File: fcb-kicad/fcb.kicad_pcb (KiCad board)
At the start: 4 copper layers, 45 x 45 mm, 90 parts, among them J1 Conn_ESC_4in1, J10 AI_5V_2, J11 AI_3V, J2 SWD, J3 Conn_Coaxial, J4 I2C, J5 USB_B_Micro, J6 PB9, J7 PB13, J8 UART, J9 AI_5V_1, Q1 S8050 J3Y, SW1 SW_Push, SW3 BTN_USER, U1 STM32F411CEUx, U2 TPS5430DDA, U3 AMS1117-3.3, U4 W25Q128JVS, U5 LSM6DS3, U6 DL-RTS4432, U7 BMP388, U8 QMC5883L, U9 USBLC6-2SC6, Y1 16 MHz

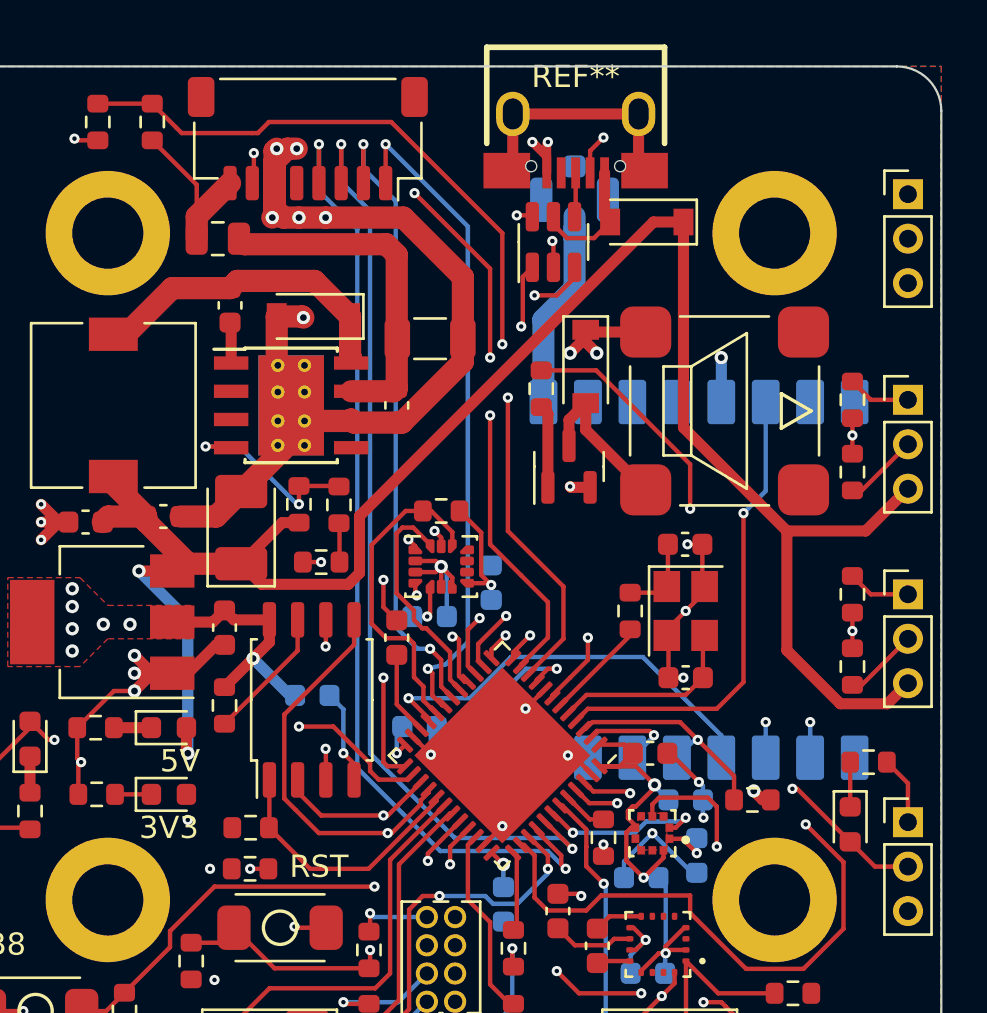
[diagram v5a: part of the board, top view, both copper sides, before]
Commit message: USB diffpair to bottom layer for more continous 3V3 fill
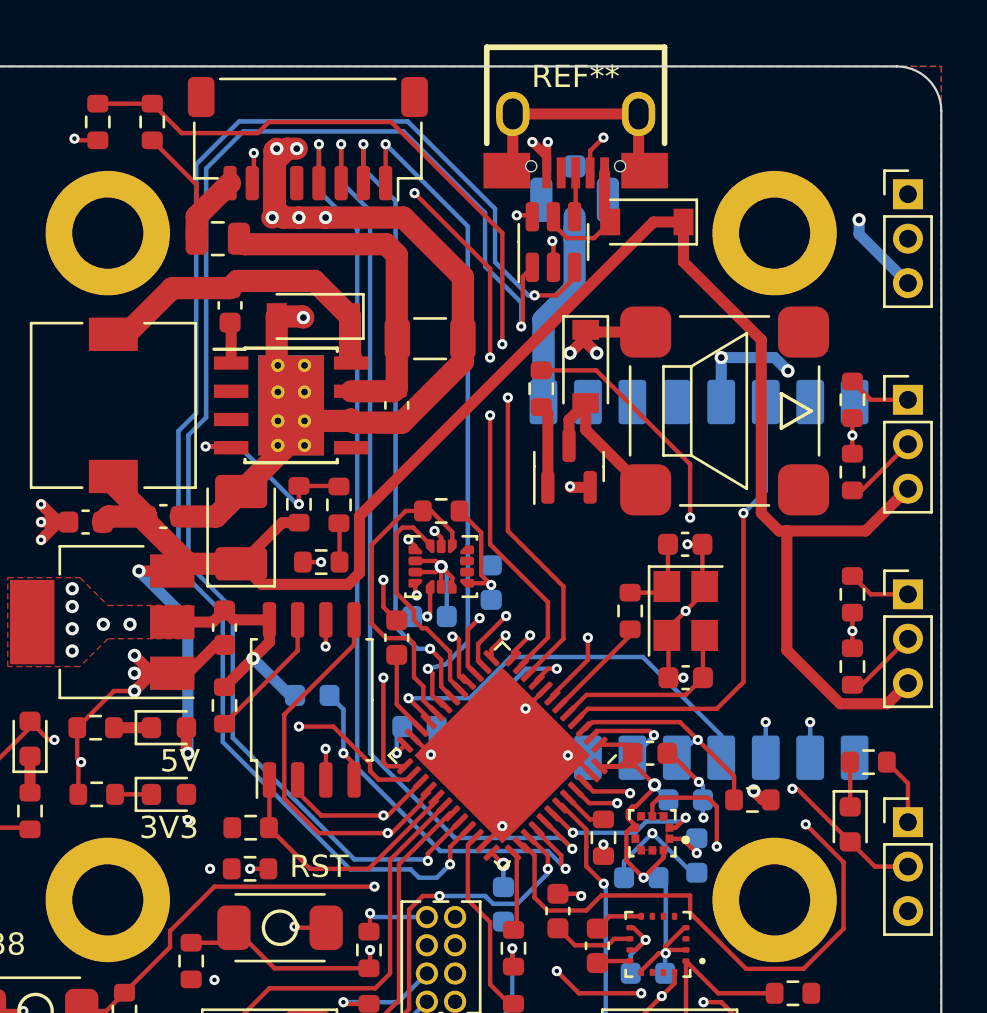
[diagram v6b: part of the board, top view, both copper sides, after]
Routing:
- net USB_D-: track 38.1 -> 63.6 mm
- net USB_D+: track 41.2 -> 65.7 mm
- net +3V3: track 70.9 -> 76.1 mm, vias 23 -> 25

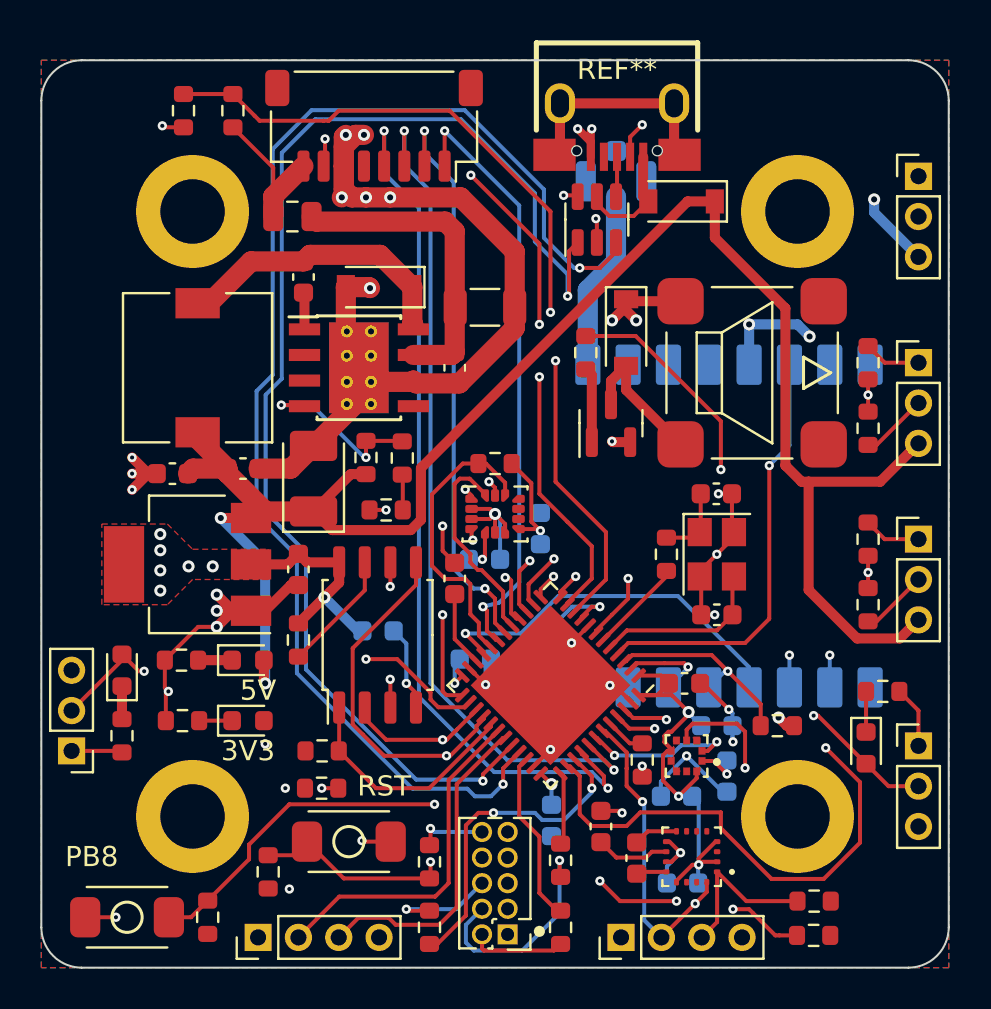
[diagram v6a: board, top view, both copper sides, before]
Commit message: Less routing on inner layers, fabrication, BOM should be OK
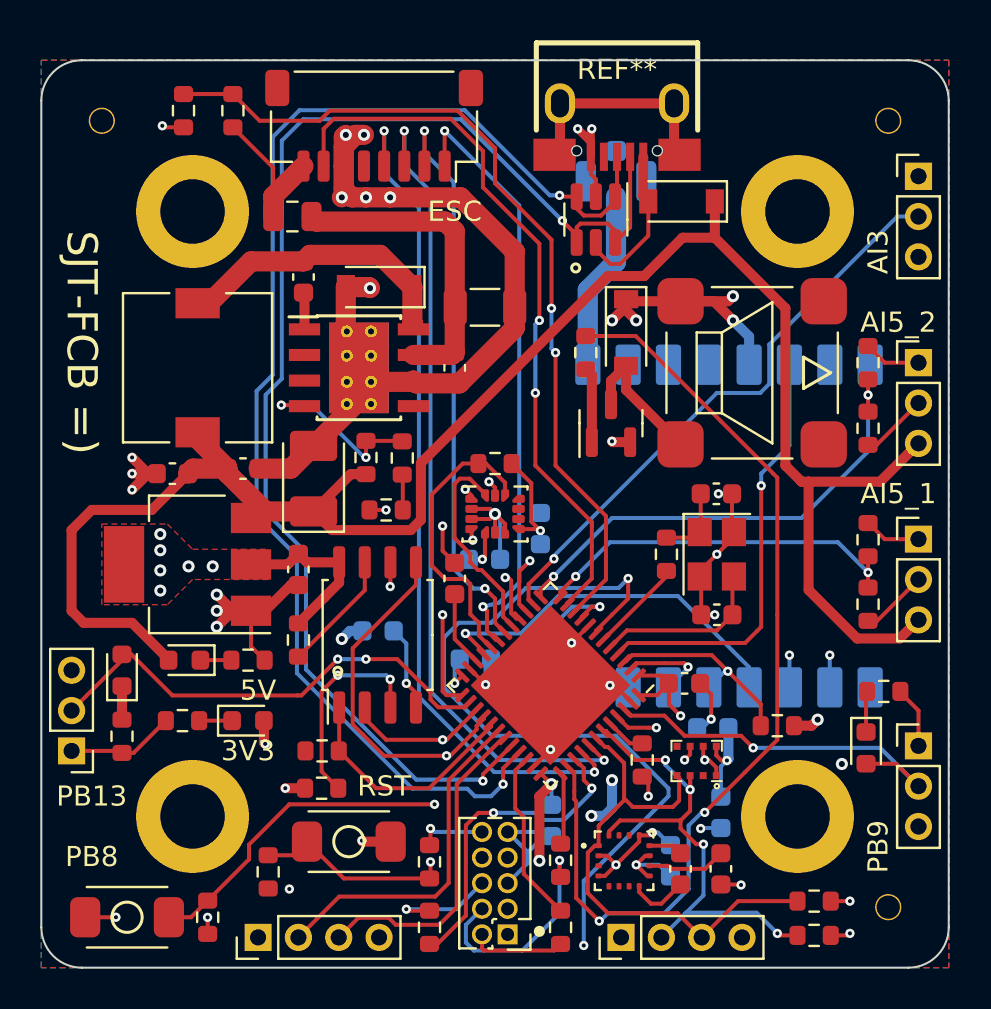
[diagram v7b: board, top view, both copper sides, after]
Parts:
- removed C17: 100n, Capacitor_SMD:C_0603_1608Metric
- removed R30: 10k, Resistor_SMD:R_0603_1608Metric
- removed SW3: BTN_USER, 000_sjt:Button-2.9x4.0mm-SMD
- added R12: 10k, Resistor_SMD:R_0603_1608Metric, F.Cu at (155.3, 114.2)
- added SW2: SW_Push, 000_sjt:Button-2.9x4.0mm-SMD, F.Cu at (129.8, 122.0)
- added T1: JLCPCB_NPTH, 000_sjt:JLCPCB_NPTH, F.Cu at (128.5, 82.5)
- added T2: JLCPCB_NPTH, 000_sjt:JLCPCB_NPTH, F.Cu at (167.5, 82.5)
- added T3: JLCPCB_NPTH, 000_sjt:JLCPCB_NPTH, F.Cu at (167.5, 121.5)
- C12, C13: value 10u -> 10u 10V
- C3: value 100n 50V -> 100n
- CL1, CL2: value 8p -> 6.8p
- J10: value AI_5V_2 -> PH1X3
- J11: value AI_3V -> PH1X3
- J4: value I2C -> PH1X4
- J6: value PB9 -> PH1X3
- J7: value PB13 -> PH1X3
- J8: value UART -> PH1X4
- J9: value AI_5V_1 -> PH1X3
- L1: value 100u 250mΩ -> 100u 650mA 250mΩ
- R10, R7, R8, R9: value 22R -> 22
- R13: value 10k -> 1k
- R15: value 1k -> 10k
- R23: value 10k -> 240
- R25: value 240 -> 470
- R26: value 470 -> 5.1k
- R27, R29: value 5k -> 10k
- R28: value 10k -> 5.1k
- U7: value BMP388 -> DPS310; footprint 000_sjt:PQFN50P200X200X80-10N -> 000_sjt:PG-VLGA-8-1
- U9: value USBLC6-2SC6 -> SRV05-4
- moved R24 37.8 mm to (129.5, 113.0), turned to -90 degrees
- moved R23 35.3 mm to (167.3, 110.8), turned to 0 degrees
- moved R22 30.1 mm to (133.8, 122.0), turned to 90 degrees
- moved R25 29.8 mm to (152.5, 94.0)
- moved R13 20.2 mm to (135.8, 109.2), turned to 0 degrees
- moved R19 19.1 mm to (162.0, 112.5)
- moved R26 18.8 mm to (166.5, 106.5), turned to 90 degrees
- moved R18 13.1 mm to (148.0, 99.5), turned to 180 degrees
- moved R20 8.89 mm to (163.8, 121.2)
- moved R17 7.44 mm to (138.2, 108.2), turned to -90 degrees
- moved R15 7.09 mm to (139.4, 113.8), turned to 0 degrees
- moved C19 6.31 mm to (159.2, 119.6), turned to -90 degrees
- moved R28 5.50 mm to (166.5, 97.8)
- moved U8 3.36 mm to (154.4, 119.2), turned to 0 degrees
- moved R29 3.25 mm to (166.5, 94.5)
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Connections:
- J5 pad 2: /IO/USB_CONN- -> USB_D-
- J5 pad 3: /IO/USB_CONN+ -> USB_D+
- R13 pad 1: CPU_BOOT0 -> Net-(D3-Pad1)
- R14 pad 1: Net-(D3-Pad1) -> Net-(D4-Pad1)
- R15 pad 1: Net-(D4-Pad1) -> +3V3
- R15 pad 2: GND -> FLASH_CS_N
- R16 pad 2: FLASH_CS_N -> Net-(R16-Pad2)
- R18 pad 2: Net-(R18-Pad2) -> IMU_CS_N
- R19 pad 2: IMU_CS_N -> RAD_CS_N
- R20 pad 2: RAD_CS_N -> I2C1_SCL
- R21 pad 2: I2C1_SCL -> I2C1_SDA
- R22 pad 2: I2C1_SDA -> GPIO_PB8
- R23 pad 1: +3V3 -> Net-(D5-Pad1)
- R23 pad 2: GPIO_PB8 -> GND
- R24 pad 1: Net-(D5-Pad1) -> Net-(D6-Pad1)
- R25 pad 1: Net-(D6-Pad1) -> BUZZER
- R25 pad 2: GND -> /IO/Q_buzzer_B
- R26 pad 1: BUZZER -> /IO/AI_5V_1
- R26 pad 2: /IO/Q_buzzer_B -> AI_5V_3V_1
- R27 pad 1: /IO/AI_5V_1 -> AI_5V_3V_1
- R27 pad 2: AI_5V_3V_1 -> GND
- R28 pad 1: AI_5V_3V_1 -> /IO/AI_5V_2
- R28 pad 2: GND -> AI_5V_3V_2
- R29 pad 1: /IO/AI_5V_2 -> AI_5V_3V_2
- R29 pad 2: AI_5V_3V_2 -> GND
- U4 pad 3: Net-(R17-Pad2) -> Net-(R16-Pad2)
- U4 pad 7: Net-(R18-Pad2) -> Net-(R17-Pad2)
- U7 pad 1: +3V3 -> GND
- U7 pad 2: I2C1_SCL -> unconnected-(U7-Pad2)
- U7 pad 3: GND -> I2C1_SDA
- U7 pad 4: I2C1_SDA -> I2C1_SCL
- U7 pad 5: GND -> unconnected-(U7-Pad5)
- U7 pad 7: unconnected-(U7-Pad7) -> GND
- U7 pad 8: GND -> +3V3
- U9 pad 1: USB_D- -> USB_D+
- U9 pad 4: /IO/USB_CONN+ -> USB_D-
- U9 pad 6: /IO/USB_CONN- -> USB_D-
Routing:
- net I2C1_SDA: track 36.5 -> 26.1 mm
- net Net-(R16-Pad2): track 0.00 -> 10.4 mm, vias 0 -> 2
- net /IO/USB_CONN-: track 8.33 -> 0.00 mm, vias 2 -> 0
- net AI_5V_3V_1: track 25.9 -> 18.8 mm
- net Net-(R18-Pad2): track 6.04 -> 0.00 mm
- net I2C1_SCL: track 31.5 -> 25.6 mm, vias 4 -> 0
- net BUZZER: track 53.6 -> 48.1 mm
- net +3V3: track 76.1 -> 71.0 mm, vias 25 -> 32
- net GND: track 136.4 -> 141.0 mm, vias 37 -> 35
- net +5V: track 87.9 -> 92.3 mm, vias 2 -> 0
- net USB_D-: track 63.6 -> 66.7 mm
- net Net-(R17-Pad2): track 9.03 -> 6.04 mm, vias 2 -> 0
- net GPIO_PB9: track 16.8 -> 19.2 mm, vias 2 -> 1
- net AI_CRNT: track 33.6 -> 36.0 mm, vias 4 -> 2
- net TIM3_CH1: track 44.1 -> 42.0 mm
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- removed copper zone on F.Cu, net GND
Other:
- rule pad_to_mask_clearance: 0 -> 0.05
- board text added: "AI3"
- board text added: "AI5_1"
- board text added: "AI5_2"
- board text added: "ESC"
- board text added: "JLCJLCJLCJLC"
- board text added: "PB13"
- board text added: "PB9"
- board text added: "SJT-FCB =)"
